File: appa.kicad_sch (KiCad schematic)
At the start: 118 parts, among them J1 USB_B, J2 USB, J3 Columns, J4 Rows, J5 I2C, J6 ICSP, SW1 SW_DIP_x01, SW10 SW_DIP_x01, SW11 SW_DIP_x01, SW12 SW_DIP_x01, SW13 SW_DIP_x01, SW14 SW_DIP_x01, SW15 SW_DIP_x01, SW16 SW_DIP_x01, SW17 SW_DIP_x01, SW18 SW_DIP_x01, SW19 SW_DIP_x01, SW2 SW_DIP_x01, SW20 SW_DIP_x01, SW21 SW_DIP_x01, SW22 SW_DIP_x01, SW23 SW_DIP_x01, SW24 SW_DIP_x01, SW25 SW_DIP_x01, SW26 SW_DIP_x01, SW27 SW_DIP_x01, SW28 SW_DIP_x01, SW29 SW_DIP_x01, SW3 SW_DIP_x01, SW30 SW_DIP_x01, SW31 SW_DIP_x01, SW32 SW_DIP_x01, SW33 SW_DIP_x01, SW34 SW_DIP_x01, SW35 SW_DIP_x01, SW36 SW_DIP_x01, SW37 SW_DIP_x01, SW38 SW_DIP_x01, SW39 SW_DIP_x01, SW4 SW_DIP_x01, SW40 SW_DIP_x01, SW41 SW_DIP_x01, SW42 SW_DIP_x01, SW43 SW_DIP_x01, SW44 SW_DIP_x01, SW45 SW_DIP_x01, SW46 SW_DIP_x01, SW47 SW_DIP_x01, SW48 SW_DIP_x01, SW49 RESET, SW5 SW_DIP_x01, SW50 BOOT, SW6 SW_DIP_x01, SW7 SW_DIP_x01, SW8 SW_DIP_x01, SW9 SW_DIP_x01, U1 ARDUINO_PRO_MINI, U2 ATmega328-P, Y1 16MHz

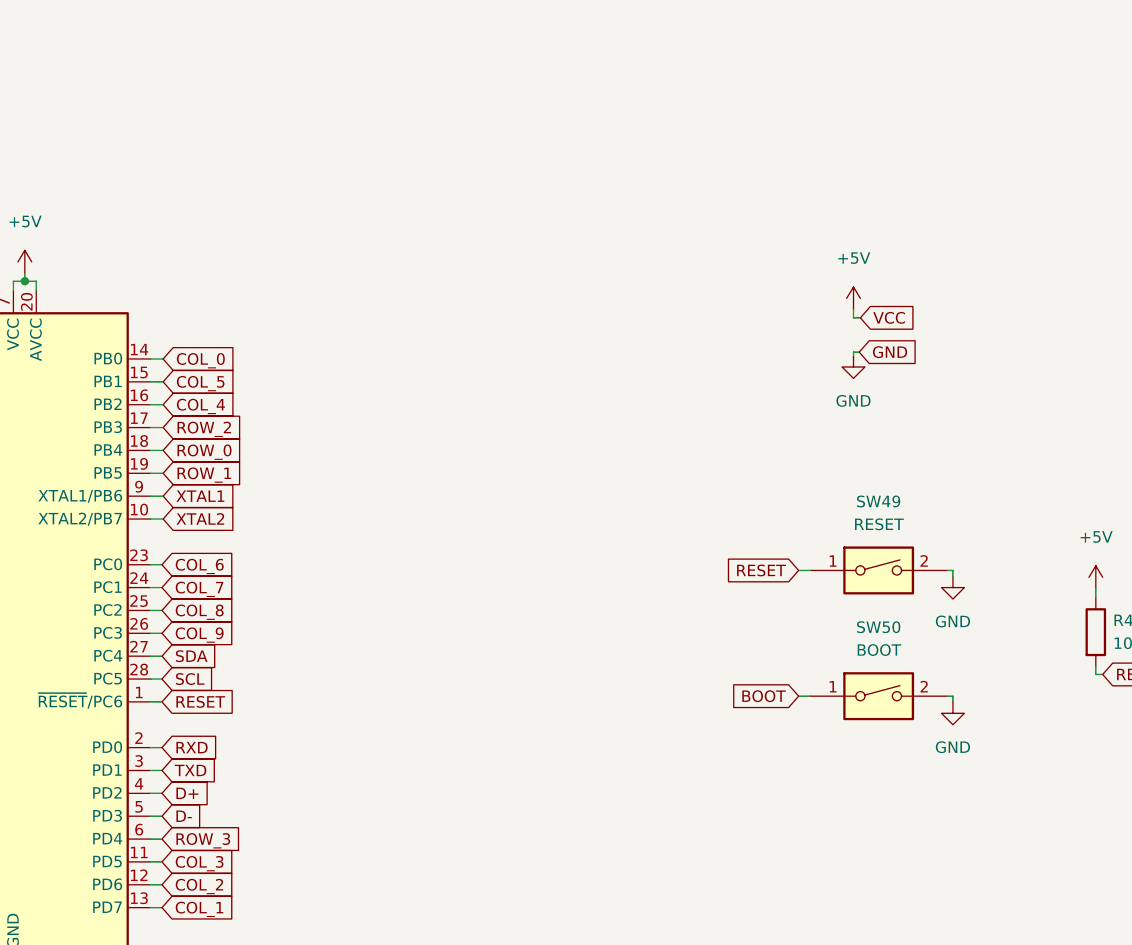
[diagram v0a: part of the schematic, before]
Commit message: Fixed unwired pins
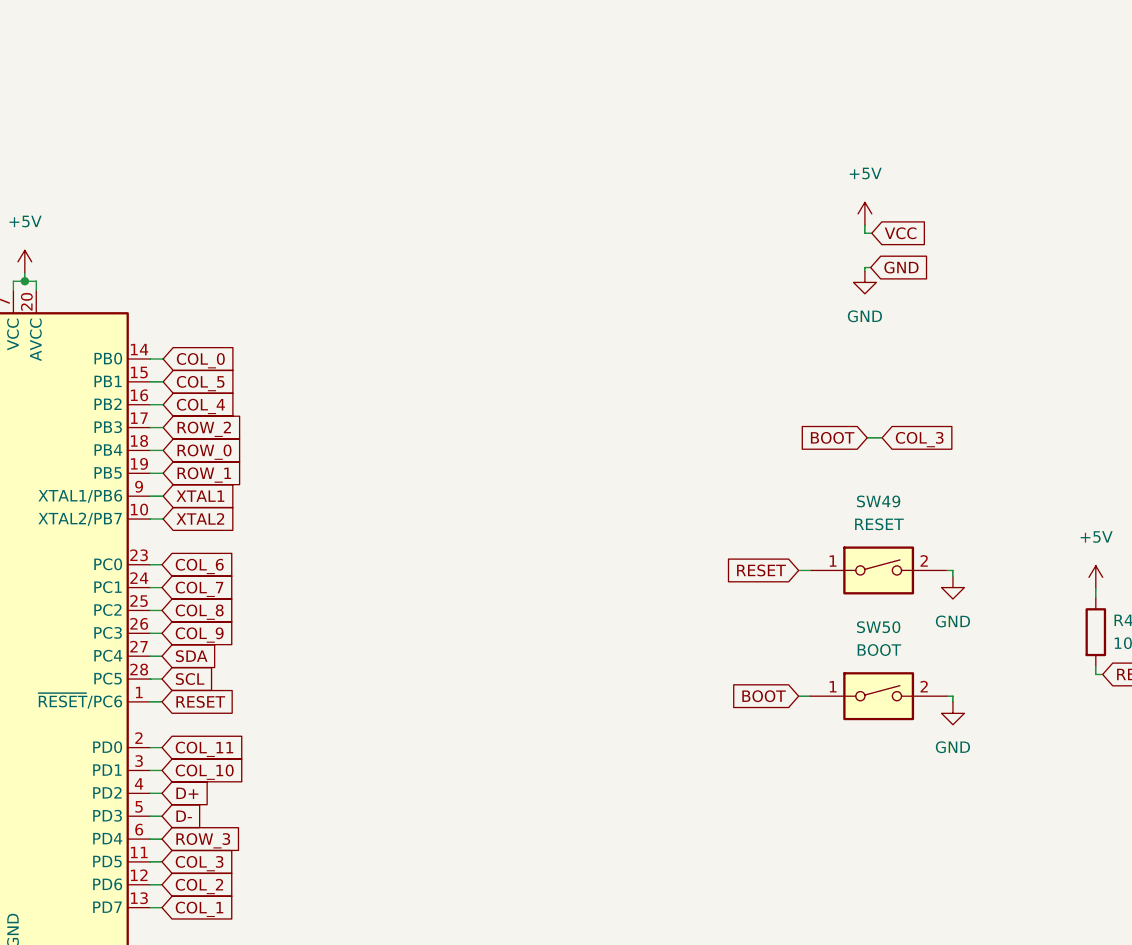
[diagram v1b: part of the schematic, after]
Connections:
- net COL_3 is gone; now on net BOOT: D13.1 (K), D14.1 (K), D15.1 (K), D16.1 (K), J3.4 (Pin_4), U1.JP7_5 (D5), U2.11 (PD5)
- net COL_10: now also U2.3 (PD1)
- net COL_11: now also U2.2 (PD0)
- net RXD: no longer U2.2 (PD0)
- net TXD: no longer U2.3 (PD1)
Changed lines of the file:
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@@
+    (stroke (width 0) (type default) (color 0 0 0 0))
+  )
+  (wire (pts (xy 326.263 211.201) (xy 327.914 211.201))
     (stroke (width 0) (type default) (color 0 0 0 0))
   )
@@
     (stroke (width 0) (type default) (color 0 0 0 0))
   )
-  (wire (pts (xy 324.739 201.676) (xy 324.739 202.057))
+  (wire (pts (xy 326.009 192.278) (xy 326.009 192.659))
     (stroke (width 0) (type default) (color 0 0 0 0))
   )
@@
     (stroke (width 0) (type default) (color 0 0 0 0))
   )
-  (wire (pts (xy 325.374 201.676) (xy 324.739 201.676))
+  (wire (pts (xy 326.644 192.278) (xy 326.009 192.278))
     (stroke (width 0) (type default) (color 0 0 0 0))
   )
@@
     (stroke (width 0) (type default) (color 0 0 0 0))
   )
-  (wire (pts (xy 324.739 196.977) (xy 324.739 197.866))
+  (wire (pts (xy 326.009 187.579) (xy 326.009 188.468))
     (stroke (width 0) (type default) (color 0 0 0 0))
   )
@@
     (stroke (width 0) (type default) (color 0 0 0 0))
   )
-  (wire (pts (xy 324.739 197.866) (xy 325.501 197.866))
+  (wire (pts (xy 326.009 188.468) (xy 326.771 188.468))
     (stroke (width 0) (type default) (color 0 0 0 0))
   )
@@
     )
   )
-  (global_label "TXD" (shape input) (at 247.904 248.158 0) (fields_autoplaced)
-    (effects (font (size 1.27 1.27)) (justify left))
-    (property "Referências entre as folhas" "${INTERSHEET_REFS}" (id 0) (at 253.7642 248.0786 0)
+  (global_label "COL_10" (shape input) (at 247.904 248.158 0) (fields_autoplaced)
+    (effects (font (size 1.27 1.27)) (justify left))
+    (property "Referências entre as folhas" "${INTERSHEET_REFS}" (id 0) (at 257.3323 248.0786 0)
       (effects (font (size 1.27 1.27)) (justify left) hide)
     )
@@
     )
   )
+  (global_label "COL_3" (shape input) (at 327.914 211.201 0) (fields_autoplaced)
+    (effects (font (size 1.27 1.27)) (justify left))
+    (property "Referências entre as folhas" "${INTERSHEET_REFS}" (id 0) (at 336.1328 211.1216 0)
+      (effects (font (size 1.27 1.27)) (justify left) hide)
+    )
+  )
   (global_label "RESET" (shape input) (at 83.82 213.995 0) (fields_autoplaced)
     (effects (font (size 1.27 1.27)) (justify left))
@@
     )
   )
-  (global_label "RXD" (shape input) (at 247.904 245.618 0) (fields_autoplaced)
-    (effects (font (size 1.27 1.27)) (justify left))
-    (property "Referências entre as folhas" "${INTERSHEET_REFS}" (id 0) (at 254.0666 245.5386 0)
+  (global_label "COL_11" (shape input) (at 247.904 245.618 0) (fields_autoplaced)
+    (effects (font (size 1.27 1.27)) (justify left))
+    (property "Referências entre as folhas" "${INTERSHEET_REFS}" (id 0) (at 257.3323 245.5386 0)
       (effects (font (size 1.27 1.27)) (justify left) hide)
     )
@@
     )
   )
-  (global_label "GND" (shape input) (at 325.374 201.676 0) (fields_autoplaced)
-    (effects (font (size 1.27 1.27)) (justify left))
-    (property "Referências entre as folhas" "${INTERSHEET_REFS}" (id 0) (at 331.6576 201.5966 0)
-      (effects (font (size 1.27 1.27)) (justify left) hide)
-    )
-  )
-  (global_label "VCC" (shape input) (at 325.501 197.866 0) (fields_autoplaced)
-    (effects (font (size 1.27 1.27)) (justify left))
-    (property "Referências entre as folhas" "${INTERSHEET_REFS}" (id 0) (at 331.5427 197.7866 0)
+  (global_label "GND" (shape input) (at 326.644 192.278 0) (fields_autoplaced)
+    (effects (font (size 1.27 1.27)) (justify left))
+    (property "Referências entre as folhas" "${INTERSHEET_REFS}" (id 0) (at 332.9276 192.1986 0)
+      (effects (font (size 1.27 1.27)) (justify left) hide)
+    )
+  )
+  (global_label "VCC" (shape input) (at 326.771 188.468 0) (fields_autoplaced)
+    (effects (font (size 1.27 1.27)) (justify left))
+    (property "Referências entre as folhas" "${INTERSHEET_REFS}" (id 0) (at 332.8127 188.3886 0)
       (effects (font (size 1.27 1.27)) (justify left) hide)
     )
@@
     )
   )
+  (global_label "BOOT" (shape input) (at 326.263 211.201 180) (fields_autoplaced)
+    (effects (font (size 1.27 1.27)) (justify right))
+    (property "Referências entre as folhas" "${INTERSHEET_REFS}" (id 0) (at 318.9513 211.1216 0)
+      (effects (font (size 1.27 1.27)) (justify right) hide)
+    )
+  )
   (global_label "COL_6" (shape input) (at 373.761 185.293 0) (fields_autoplaced)
     (effects (font (size 1.27 1.27)) (justify left))
@@
     )
   )
-  (symbol (lib_id "power:+5V") (at 324.739 196.977 0) (unit 1)
-    (in_bom yes) (on_board yes) (fields_autoplaced)
-    (property "Reference" "#PWR0117" (id 0) (at 324.739 200.787 0)
-      (effects (font (size 1.27 1.27)) hide)
-    )
-    (property "Value" "+5V" (id 1) (at 324.739 191.262 0))
-    (property "Footprint" "" (id 2) (at 324.739 196.977 0)
-      (effects (font (size 1.27 1.27)) hide)
-    )
-    (property "Datasheet" "" (id 3) (at 324.739 196.977 0)
+  (symbol (lib_id "power:+5V") (at 326.009 187.579 0) (unit 1)
+    (in_bom yes) (on_board yes) (fields_autoplaced)
+    (property "Reference" "#PWR0117" (id 0) (at 326.009 191.389 0)
+      (effects (font (size 1.27 1.27)) hide)
+    )
+    (property "Value" "+5V" (id 1) (at 326.009 181.864 0))
+    (property "Footprint" "" (id 2) (at 326.009 187.579 0)
+      (effects (font (size 1.27 1.27)) hide)
+    )
+    (property "Datasheet" "" (id 3) (at 326.009 187.579 0)
       (effects (font (size 1.27 1.27)) hide)
     )
@@
     (pin "2")
   )
-  (symbol (lib_id "power:GND") (at 324.739 202.057 0) (unit 1)
-    (in_bom yes) (on_board yes) (fields_autoplaced)
-    (property "Reference" "#PWR0121" (id 0) (at 324.739 208.407 0)
-      (effects (font (size 1.27 1.27)) hide)
-    )
-    (property "Value" "GND" (id 1) (at 324.739 207.137 0))
-    (property "Footprint" "" (id 2) (at 324.739 202.057 0)
-      (effects (font (size 1.27 1.27)) hide)
-    )
-    (property "Datasheet" "" (id 3) (at 324.739 202.057 0)
-      (effects (font (size 1.27 1.27)) hide)
-    )
+  (symbol (lib_id "power:GND") (at 326.009 192.659 0) (unit 1)
+    (in_bom yes) (on_board yes) (fields_autoplaced)
+    (property "Reference" "#PWR0121" (id 0) (at 326.009 199.009 0)
+      (effects (font (size 1.27 1.27)) hide)
+    )
+    (property "Value" "GND" (id 1) (at 326.009 197.739 0))
+    (property "Footprint" "" (id 2) (at 326.009 192.659 0)
+      (effects (font (size 1.27 1.27)) hide)
+    )
+    (property "Datasheet" "" (id 3) (at 326.009 192.659 0)
+      (effects (font (size 1.27 1.27)) hide)
+    )
